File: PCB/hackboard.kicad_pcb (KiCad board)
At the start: 2 copper layers, 436.6 x 131.8 mm, 208 parts

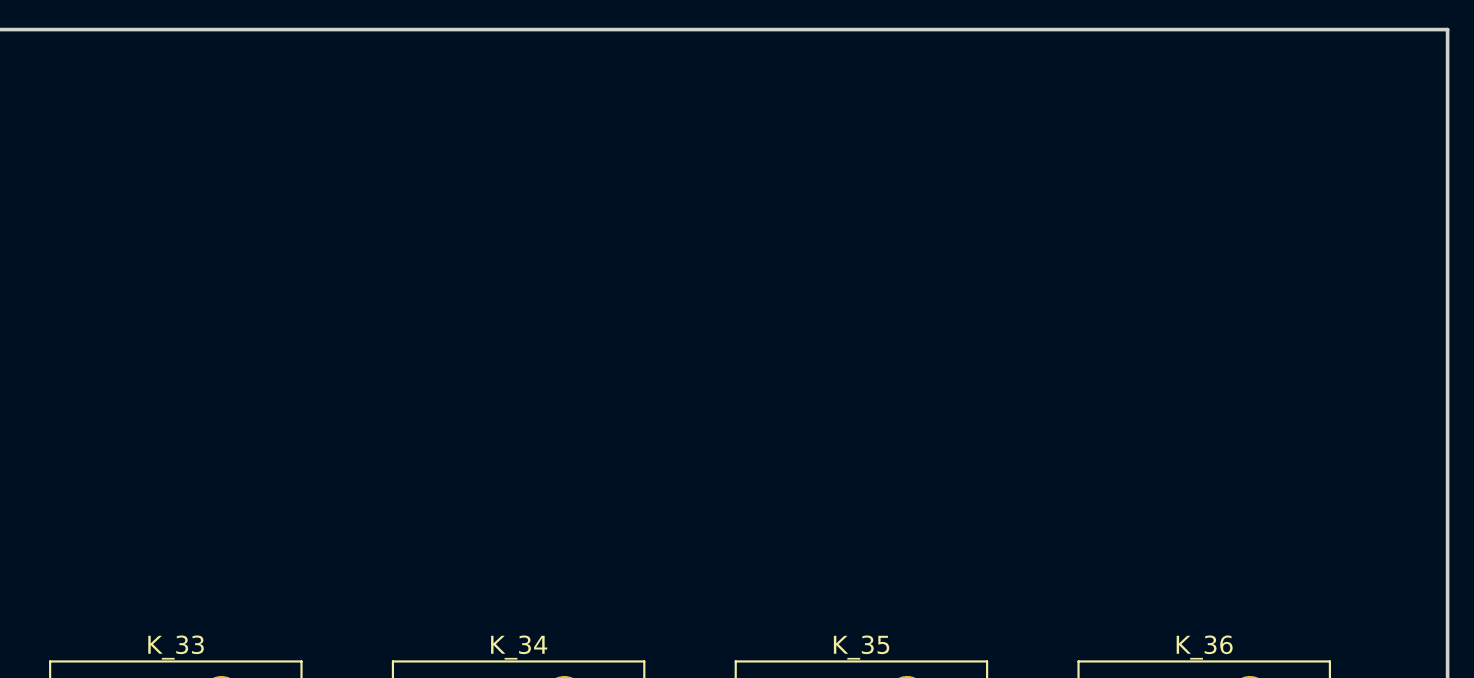
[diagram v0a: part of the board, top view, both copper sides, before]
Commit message: add submodules for pi pico, files for oled
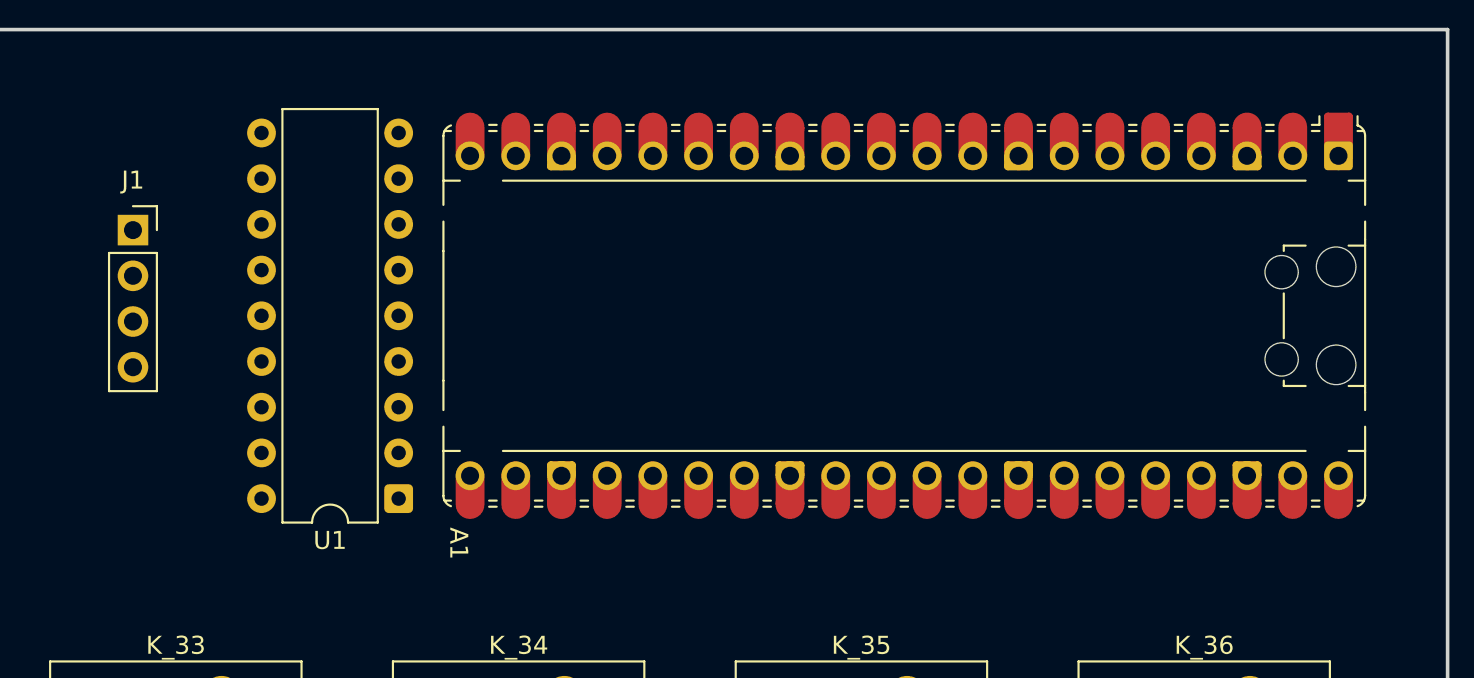
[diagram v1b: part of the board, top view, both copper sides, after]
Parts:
- added A1: RaspberryPi_Pico, Module:RaspberryPi_Pico_Common_Unspecified, F.Cu at (450.1, 90.5)
- added J1: Conn_01x04, Connector_PinSocket_2.54mm:PinSocket_1x04_P2.54mm_Vertical, F.Cu at (407.2, 85.7)
- added U1: MCP23008-xP, Package_DIP:DIP-18_W7.62mm, F.Cu at (422.0, 100.6)
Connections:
- K_102 pad 1: col19 -> col18
- K_103 pad 1: col21 -> col20
- K_33 pad 1: col19 -> col18
- K_34 pad 1: col20 -> col19
- K_35 pad 1: col21 -> col20
- K_36 pad 1: col22 -> col21
- K_54 pad 1: col19 -> col18
- K_55 pad 1: col20 -> col19
- K_56 pad 1: col21 -> col20
- K_57 pad 1: col22 -> col21
- K_71 pad 1: col19 -> col18
- K_72 pad 1: col20 -> col19
- K_73 pad 1: col21 -> col20
- K_87 pad 1: col19 -> col18
- K_88 pad 1: col20 -> col19
- K_89 pad 1: col21 -> col20
- K_90 pad 1: col22 -> col21

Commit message: add pcb routing and 3d model
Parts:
- K_0, K_1, K_10, K_100, K_101, K_103, K_11, K_12, K_13, K_14, K_15, K_16, K_17, K_18, K_19, K_2, K_20, K_21, K_22, K_23, K_24, K_25, K_26, K_27, K_28, K_3, K_30, K_31, K_32, K_33, K_34, K_35, K_36, K_38, K_39, K_4, K_40, K_41, K_42, K_43, K_44, K_45, K_46, K_47, K_48, K_49, K_5, K_51, K_52, K_53, K_54, K_55, K_56, K_59, K_6, K_60, K_61, K_62, K_63, K_64, K_65, K_66, K_67, K_68, K_69, K_7, K_71, K_72, K_73, K_75, K_76, K_77, K_78, K_79, K_8, K_80, K_81, K_82, K_83, K_84, K_86, K_87, K_88, K_89, K_9, K_99: footprint Button_Switch_Keyboard:SW_Cherry_MX_1.00u_PCB -> Library_Edited:SW_Cherry_MX_1.00u_PCB
- moved J1 2.38 mm to (404.8, 85.7)
- moved U1 2.38 mm to (419.6, 100.6)
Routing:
- net col0: track 0.00 -> 529.1 mm, vias 0 -> 1
- net row4: track 0.00 -> 494.2 mm
- net col1: track 0.00 -> 486.9 mm, vias 0 -> 2
- net row2: track 0.00 -> 467.3 mm
- net row3: track 0.00 -> 465.8 mm
- net col3: track 0.00 -> 460.0 mm
- net col2: track 0.00 -> 456.9 mm
- net row1: track 0.00 -> 454.4 mm
- net row0: track 0.00 -> 429.2 mm, vias 0 -> 1
- net col4: track 0.00 -> 413.3 mm
- net row5: track 0.00 -> 391.3 mm
- net col5: track 0.00 -> 388.8 mm
- net col6: track 0.00 -> 384.3 mm, vias 0 -> 1
- net col7: track 0.00 -> 360.3 mm
- net col8: track 0.00 -> 338.5 mm
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
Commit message: add 3d models for all key switches and components
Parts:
- A1: footprint Module:RaspberryPi_Pico_Common_Unspecified -> Library_Edited:RaspberryPi_Pico_Common_Unspecified
- J1: footprint Connector_PinSocket_2.54mm:PinSocket_1x04_P2.54mm_Vertical -> Library_Edited:PinSocket_1x04_P2.54mm_Vertical_OLED
- K_102, K_29, K_57, K_90: footprint Button_Switch_Keyboard:SW_Cherry_MX_2.00u_PCB -> Library_Edited:SW_Cherry_MX_2.00u_PCB
- K_37, K_50: footprint Button_Switch_Keyboard:SW_Cherry_MX_1.50u_PCB -> Library_Edited:SW_Cherry_MX_1.50u_PCB
- K_58: footprint Button_Switch_Keyboard:SW_Cherry_MX_1.75u_PCB -> Library_Edited:SW_Cherry_MX_1.75u_PCB
- K_70, K_74: footprint Button_Switch_Keyboard:SW_Cherry_MX_2.25u_PCB -> Library_Edited:SW_Cherry_MX_2.25u_PCB
- K_85: footprint Button_Switch_Keyboard:SW_Cherry_MX_2.75u_PCB -> Library_Edited:SW_Cherry_MX_2.75u_PCB
- K_91, K_92, K_93, K_95, K_96, K_97, K_98: footprint Button_Switch_Keyboard:SW_Cherry_MX_1.25u_PCB -> Library_Edited:SW_Cherry_MX_1.25u_PCB
- K_94: footprint Button_Switch_Keyboard:SW_Cherry_MX_6.25u_PCB -> Library_Edited:SW_Cherry_MX_6.25u_PCB
- moved A1 4.43 mm to (454.5, 90.0)
- moved U1 1.04 mm to (420.6, 100.6)
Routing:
- net col1: track 486.9 -> 498.5 mm
- net col6: track 384.3 -> 395.7 mm
- net col20: track 134.7 -> 125.6 mm
- net row2: track 467.3 -> 476.0 mm, vias 0 -> 1
- net col14: track 258.7 -> 250.8 mm, vias 0 -> 1
- net i2c1_scl: track 42.6 -> 49.7 mm
- net col9: track 311.3 -> 318.2 mm
- net col5: track 388.8 -> 395.5 mm
- net col4: track 413.3 -> 419.8 mm
- net col0: track 529.1 -> 534.4 mm
- net col3: track 460.0 -> 465.1 mm
- net row4: track 494.2 -> 499.2 mm
- net i2c1_sda: track 39.1 -> 44.1 mm
- net col12: track 232.0 -> 236.9 mm
- net col13: track 264.0 -> 268.8 mm
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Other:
- board text added: "By Allen Ding - github.com/ading2210"
- board text added: "colon3board :3"
- board text added: "v1.0"

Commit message: silkscreen art and mounting holes
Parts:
- added G***: LOGO, LOGO, B.Cu at (389.0, 173.0)
- added G***: LOGO, LOGO, B.Cu at (352.0, 158.0)
- added REF**: MountingHole_2.2mm_M2, MountingHole:MountingHole_2.2mm_M2, F.Cu at (46.0, 77.0)
- added REF**: MountingHole_2.2mm_M2, MountingHole:MountingHole_2.2mm_M2, F.Cu at (252.6, 204.0)
- added REF**: MountingHole_2.2mm_M2, MountingHole:MountingHole_2.2mm_M2, F.Cu at (477.9, 104.1)
- added REF**: MountingHole_2.2mm_M2, MountingHole:MountingHole_2.2mm_M2, F.Cu at (46.0, 204.0)
- added REF**: MountingHole_2.2mm_M2, MountingHole:MountingHole_2.2mm_M2, F.Cu at (477.9, 204.0)
- added REF**: MountingHole_2.2mm_M2, MountingHole:MountingHole_2.2mm_M2, F.Cu at (252.6, 101.1)
- K_57, K_90: footprint Library_Edited:SW_Cherry_MX_2.00u_PCB -> Library_Edited:SW_Cherry_MX_2.00u_PCB_r1
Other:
- board text added: "Source code:"
- board text added: "blahaj :3"

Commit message: fix missing row5 connection on pcb
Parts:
- renumbered G*** to G1, G*** to G2, REF** to H1, REF** to H2, REF** to H3, REF** to H4, REF** to H5, REF** to H6
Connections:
- A1 pad 10: col2 -> col1
- A1 pad 11: col3 -> col2
- A1 pad 12: col4 -> col3
- A1 pad 14: col5 -> col4
- A1 pad 15: col6 -> col5
- A1 pad 16: col7 -> col6
- A1 pad 17: col8 -> col7
- A1 pad 19: col9 -> col8
- A1 pad 20: col10 -> col9
- A1 pad 26: col11 -> col10
- A1 pad 27: col12 -> col11
- A1 pad 29: col13 -> col12
- A1 pad 31: col14 -> col13
- A1 pad 32: col15 -> col14
- A1 pad 34: col16 -> col15
- A1 pad 7: col0 -> row5
- A1 pad 9: col1 -> col0
- U1 pad 10: col17 -> col16
- U1 pad 11: col18 -> col17
- U1 pad 12: col19 -> col18
- U1 pad 13: col20 -> col19
- U1 pad 14: col21 -> col20
- U1 pad 15: unconnected-(U1-GP5-Pad15) -> col21
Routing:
- net row5: track 391.3 -> 517.0 mm
- net col16: track 204.8 -> 149.8 mm
- net col13: track 268.8 -> 292.5 mm
- net col0: track 534.4 -> 514.7 mm, vias 1 -> 0
- net col6: track 395.7 -> 380.4 mm
- net row0: track 430.5 -> 417.9 mm, vias 1 -> 0
- net col10: track 312.2 -> 322.4 mm, vias 0 -> 1
- net col4: track 419.8 -> 410.2 mm
- net col1: track 498.5 -> 489.0 mm, vias 2 -> 1
- net col11: track 294.2 -> 303.1 mm
- net i2c1_scl: track 49.7 -> 41.6 mm
- net row2: track 476.0 -> 468.1 mm, vias 1 -> 0
- net col5: track 395.5 -> 388.2 mm
- net col8: track 340.7 -> 333.4 mm
- net col9: track 318.2 -> 311.2 mm
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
